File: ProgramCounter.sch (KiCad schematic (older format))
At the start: 8 parts, among them U13 74LS245, U14 74LS245, U15 74LS161, U16 74LS161, U17 74LS161, U18 74LS161

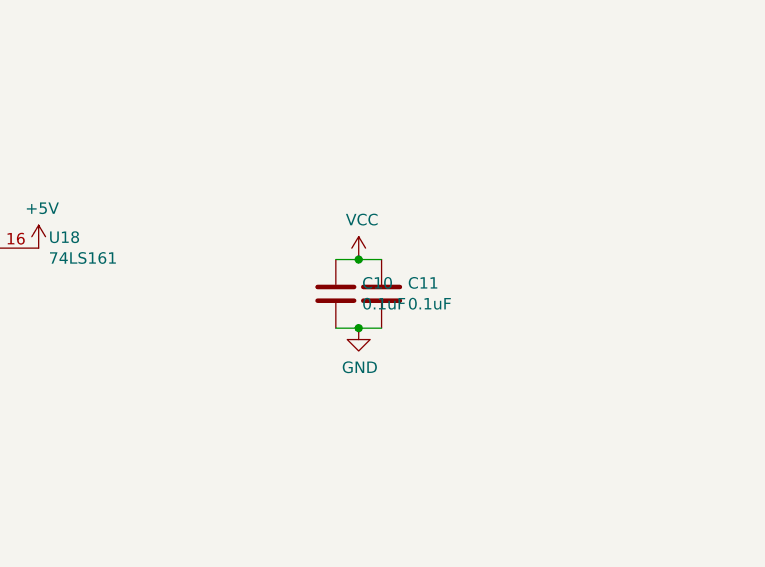
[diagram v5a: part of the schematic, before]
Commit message: added display
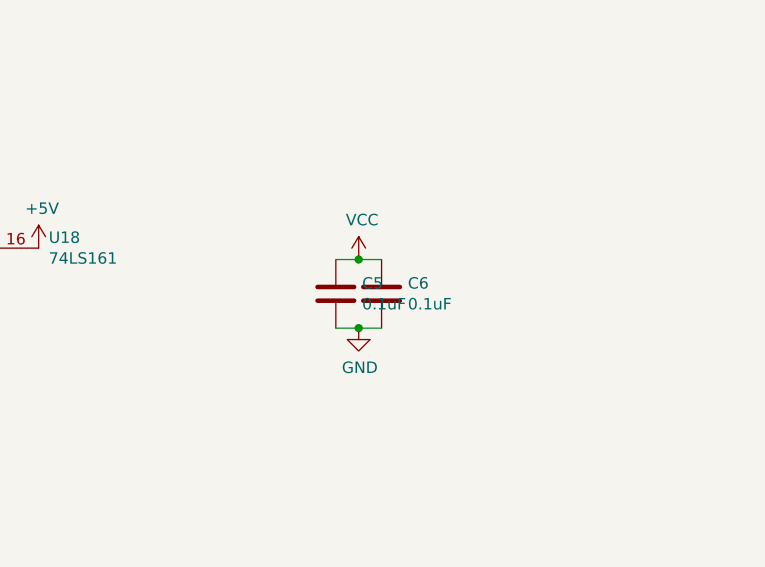
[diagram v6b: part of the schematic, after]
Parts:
- renumbered C10 to C5, C11 to C6
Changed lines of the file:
@@
 $Descr A3 16535 11693
 encoding utf-8
-Sheet 6 22
+Sheet 6 23
 Title ""
 Date ""
@@
 AR Path="/603B766D/5F6D5FCC" Ref="#PWR?"  Part="1"
 AR Path="/5F74778C/5F6D5FCC" Ref="#PWR?"  Part="1"
-AR Path="/5F6ACD14/5F6D5FCC" Ref="#PWR072"  Part="1"
-F 0 "#PWR072" H 4750 4200 50  0001 C CNN
+AR Path="/5F6ACD14/5F6D5FCC" Ref="#PWR050"  Part="1"
+F 0 "#PWR050" H 4750 4200 50  0001 C CNN
 F 1 "GND" H 4755 4277 50  0000 C CNN
 F 2 "" H 4750 4450 50  0001 C CNN
@@
 AR Path="/603B766D/5F6D5FF6" Ref="#PWR?"  Part="1"
 AR Path="/5F74778C/5F6D5FF6" Ref="#PWR?"  Part="1"
-AR Path="/5F6ACD14/5F6D5FF6" Ref="#PWR070"  Part="1"
-F 0 "#PWR070" H 3150 4300 50  0001 C CNN
+AR Path="/5F6ACD14/5F6D5FF6" Ref="#PWR048"  Part="1"
+F 0 "#PWR048" H 3150 4300 50  0001 C CNN
 F 1 "+5V" H 3165 4623 50  0000 C CNN
 F 2 "" H 3150 4450 50  0001 C CNN
@@
 AR Path="/603B766D/5F6D60A0" Ref="#PWR?"  Part="1"
 AR Path="/5F74778C/5F6D60A0" Ref="#PWR?"  Part="1"
-AR Path="/5F6ACD14/5F6D60A0" Ref="#PWR073"  Part="1"
-F 0 "#PWR073" H 4750 4200 50  0001 C CNN
+AR Path="/5F6ACD14/5F6D60A0" Ref="#PWR051"  Part="1"
+F 0 "#PWR051" H 4750 4200 50  0001 C CNN
 F 1 "GND" H 4755 4277 50  0000 C CNN
 F 2 "" H 4750 4450 50  0001 C CNN
@@
 AR Path="/603B766D/5F6D60B8" Ref="#PWR?"  Part="1"
 AR Path="/5F74778C/5F6D60B8" Ref="#PWR?"  Part="1"
-AR Path="/5F6ACD14/5F6D60B8" Ref="#PWR069"  Part="1"
-F 0 "#PWR069" H 3150 3400 50  0001 C CNN
+AR Path="/5F6ACD14/5F6D60B8" Ref="#PWR047"  Part="1"
+F 0 "#PWR047" H 3150 3400 50  0001 C CNN
 F 1 "GND" H 3155 3477 50  0000 C CNN
 F 2 "" H 3150 3650 50  0001 C CNN
@@
 AR Path="/603B766D/5F6D60C4" Ref="#PWR?"  Part="1"
 AR Path="/5F74778C/5F6D60C4" Ref="#PWR?"  Part="1"
-AR Path="/5F6ACD14/5F6D60C4" Ref="#PWR066"  Part="1"
-F 0 "#PWR066" H 1550 3500 50  0001 C CNN
+AR Path="/5F6ACD14/5F6D60C4" Ref="#PWR045"  Part="1"
+F 0 "#PWR045" H 1550 3500 50  0001 C CNN
 F 1 "+5V" H 1565 3823 50  0000 C CNN
 F 2 "" H 1550 3650 50  0001 C CNN
@@
 AR Path="/603B766D/5F6D60D0" Ref="#PWR?"  Part="1"
 AR Path="/5F74778C/5F6D60D0" Ref="#PWR?"  Part="1"
-AR Path="/5F6ACD14/5F6D60D0" Ref="#PWR071"  Part="1"
-F 0 "#PWR071" H 3150 4300 50  0001 C CNN
+AR Path="/5F6ACD14/5F6D60D0" Ref="#PWR049"  Part="1"
+F 0 "#PWR049" H 3150 4300 50  0001 C CNN
 F 1 "+5V" H 3165 4623 50  0000 C CNN
 F 2 "" H 3150 4450 50  0001 C CNN
@@
 AR Path="/603B766D/5F6D6186" Ref="#PWR?"  Part="1"
 AR Path="/5F74778C/5F6D6186" Ref="#PWR?"  Part="1"
-AR Path="/5F6ACD14/5F6D6186" Ref="#PWR067"  Part="1"
-F 0 "#PWR067" H 1550 3500 50  0001 C CNN
+AR Path="/5F6ACD14/5F6D6186" Ref="#PWR046"  Part="1"
+F 0 "#PWR046" H 1550 3500 50  0001 C CNN
 F 1 "+5V" H 1565 3823 50  0000 C CNN
 F 2 "" H 1550 3650 50  0001 C CNN
@@
 P 6900 4250
 AR Path="/5F9A8E46" Ref="#PWR?"  Part="1"
-AR Path="/5F6ACD14/5F9A8E46" Ref="#PWR075"  Part="1"
-F 0 "#PWR075" H 6900 4100 50  0001 C CNN
+AR Path="/5F6ACD14/5F9A8E46" Ref="#PWR053"  Part="1"
+F 0 "#PWR053" H 6900 4100 50  0001 C CNN
 F 1 "+5V" H 6915 4423 50  0000 C CNN
 F 2 "" H 6900 4250 50  0001 C CNN
@@
 P 8850 4400
 AR Path="/5F9B1DDA" Ref="#PWR?"  Part="1"
-AR Path="/5F6ACD14/5F9B1DDA" Ref="#PWR077"  Part="1"
-F 0 "#PWR077" H 8850 4250 50  0001 C CNN
+AR Path="/5F6ACD14/5F9B1DDA" Ref="#PWR055"  Part="1"
+F 0 "#PWR055" H 8850 4250 50  0001 C CNN
 F 1 "+5V" H 8865 4573 50  0000 C CNN
 F 2 "" H 8850 4400 50  0001 C CNN
@@
 P 10700 4450
 AR Path="/5F9BCAE2" Ref="#PWR?"  Part="1"
-AR Path="/5F6ACD14/5F9BCAE2" Ref="#PWR079"  Part="1"
-F 0 "#PWR079" H 10700 4300 50  0001 C CNN
+AR Path="/5F6ACD14/5F9BCAE2" Ref="#PWR057"  Part="1"
+F 0 "#PWR057" H 10700 4300 50  0001 C CNN
 F 1 "+5V" H 10715 4623 50  0000 C CNN
 F 2 "" H 10700 4450 50  0001 C CNN
@@
 P 12550 4450
 AR Path="/5F9BD87F" Ref="#PWR?"  Part="1"
-AR Path="/5F6ACD14/5F9BD87F" Ref="#PWR081"  Part="1"
-F 0 "#PWR081" H 12550 4300 50  0001 C CNN
+AR Path="/5F6ACD14/5F9BD87F" Ref="#PWR059"  Part="1"
+F 0 "#PWR059" H 12550 4300 50  0001 C CNN
 F 1 "+5V" H 12565 4623 50  0000 C CNN
 F 2 "" H 12550 4450 50  0001 C CNN
@@
 P 5300 4450
 AR Path="/5F9BEDE2" Ref="#PWR?"  Part="1"
-AR Path="/5F6ACD14/5F9BEDE2" Ref="#PWR074"  Part="1"
-F 0 "#PWR074" H 5300 4200 50  0001 C CNN
+AR Path="/5F6ACD14/5F9BEDE2" Ref="#PWR052"  Part="1"
+F 0 "#PWR052" H 5300 4200 50  0001 C CNN
 F 1 "GND" H 5305 4277 50  0000 C CNN
 F 2 "" H 5300 4450 50  0001 C CNN
@@
 P 7250 4450
 AR Path="/5F9C426E" Ref="#PWR?"  Part="1"
-AR Path="/5F6ACD14/5F9C426E" Ref="#PWR076"  Part="1"
-F 0 "#PWR076" H 7250 4200 50  0001 C CNN
+AR Path="/5F6ACD14/5F9C426E" Ref="#PWR054"  Part="1"
+F 0 "#PWR054" H 7250 4200 50  0001 C CNN
 F 1 "GND" H 7255 4277 50  0000 C CNN
 F 2 "" H 7250 4450 50  0001 C CNN
@@
 P 9100 4450
 AR Path="/5F9CE333" Ref="#PWR?"  Part="1"
-AR Path="/5F6ACD14/5F9CE333" Ref="#PWR078"  Part="1"
-F 0 "#PWR078" H 9100 4200 50  0001 C CNN
+AR Path="/5F6ACD14/5F9CE333" Ref="#PWR056"  Part="1"
+F 0 "#PWR056" H 9100 4200 50  0001 C CNN
 F 1 "GND" H 9105 4277 50  0000 C CNN
 F 2 "" H 9100 4450 50  0001 C CNN
@@
 P 10950 4450
 AR Path="/5F9D8AA1" Ref="#PWR?"  Part="1"
-AR Path="/5F6ACD14/5F9D8AA1" Ref="#PWR080"  Part="1"
-F 0 "#PWR080" H 10950 4200 50  0001 C CNN
+AR Path="/5F6ACD14/5F9D8AA1" Ref="#PWR058"  Part="1"
+F 0 "#PWR058" H 10950 4200 50  0001 C CNN
 F 1 "GND" H 10955 4277 50  0000 C CNN
 F 2 "" H 10950 4450 50  0001 C CNN
@@
 P 13950 4500
 AR Path="/5FB038A7" Ref="#PWR?"  Part="1"
-AR Path="/5F6ACD14/5FB038A7" Ref="#PWR0263"  Part="1"
-F 0 "#PWR0263" H 13950 4350 50  0001 C CNN
+AR Path="/5F6ACD14/5FB038A7" Ref="#PWR060"  Part="1"
+F 0 "#PWR060" H 13950 4350 50  0001 C CNN
 F 1 "VCC" H 13965 4673 50  0000 C CNN
 F 2 "" H 13950 4500 50  0001 C CNN
@@
 AR Path="/5FB038AD" Ref="#PWR?"  Part="1"
 AR Path="/5F75E433/5FB038AD" Ref="#PWR?"  Part="1"
-AR Path="/5F6ACD14/5FB038AD" Ref="#PWR0264"  Part="1"
-F 0 "#PWR0264" H 13950 4550 50  0001 C CNN
+AR Path="/5F6ACD14/5FB038AD" Ref="#PWR061"  Part="1"
+F 0 "#PWR061" H 13950 4550 50  0001 C CNN
 F 1 "GND" H 13955 4627 50  0000 C CNN
 F 2 "" H 13950 4800 50  0001 C CNN
@@
 P 13850 4650
 AR Path="/5F75E433/5FB038B5" Ref="C?"  Part="1"
-AR Path="/5F6ACD14/5FB038B5" Ref="C10"  Part="1"
-F 0 "C10" H 13965 4696 50  0000 L CNN
+AR Path="/5F6ACD14/5FB038B5" Ref="C5"  Part="1"
+F 0 "C5" H 13965 4696 50  0000 L CNN
 F 1 "0.1uF" H 13965 4605 50  0000 L CNN
 F 2 "Capacitor_THT:CP_Axial_L10.0mm_D4.5mm_P15.00mm_Horizontal" H 13888 4500 50  0001 C CNN
@@
 P 14050 4650
 AR Path="/5F75E433/5FB038BF" Ref="C?"  Part="1"
-AR Path="/5F6ACD14/5FB038BF" Ref="C11"  Part="1"
-F 0 "C11" H 14165 4696 50  0000 L CNN
+AR Path="/5F6ACD14/5FB038BF" Ref="C6"  Part="1"
+F 0 "C6" H 14165 4696 50  0000 L CNN
 F 1 "0.1uF" H 14165 4605 50  0000 L CNN
 F 2 "Capacitor_THT:CP_Axial_L10.0mm_D4.5mm_P15.00mm_Horizontal" H 14088 4500 50  0001 C CNN

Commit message: clean up
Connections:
- wire segments 243 -> 222
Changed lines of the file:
@@
 Wire Wire Line
 	9400 2750 11250 2750
-Connection ~ 11250 2750
-Wire Wire Line
-	11250 2750 15650 2750
 Wire Wire Line
 	1150 2750 5600 2750
@@
 Wire Wire Line
 	11750 3950 11750 2650
-Connection ~ 11750 2650
-Wire Wire Line
-	11750 2650 15650 2650
 Wire Wire Line
 	5800 3950 5800 750
-Connection ~ 5800 750
-Wire Wire Line
-	5800 750  15650 750
 Text HLabel 1150 2850 0    50   Input ~ 0
 CE
@@
 Wire Wire Line
 	11650 3900 11650 3950
-Connection ~ 11600 2850
-Wire Wire Line
-	11600 2850 15650 2850
 Wire Wire Line
 	11600 3900 11550 3900
@@
 Wire Wire Line
 	4450 5150 4450 4950
-Connection ~ 5050 2950
-Wire Wire Line
-	5050 2950 15650 2950
 Wire Wire Line
 	6600 3950 6600 1000
-Connection ~ 6600 1000
-Wire Wire Line
-	6600 1000 15650 1000
 Wire Wire Line
 	6500 3950 6500 1100
-Connection ~ 6500 1100
-Wire Wire Line
-	6500 1100 15650 1100
 Wire Wire Line
 	6400 3950 6400 1200
-Connection ~ 6400 1200
-Wire Wire Line
-	6400 1200 15650 1200
 Wire Wire Line
 	6300 3950 6300 1300
-Connection ~ 6300 1300
-Wire Wire Line
-	6300 1300 15650 1300
-Connection ~ 8550 1400
 Wire Wire Line
 	8450 1500 8450 3950
-Connection ~ 8450 1500
-Wire Wire Line
-	8450 1500 15650 1500
 Wire Wire Line
 	8350 1600 8350 3950
-Connection ~ 8350 1600
-Wire Wire Line
-	8350 1600 15650 1600
 Connection ~ 8550 3950
 Wire Wire Line
@@
 Wire Wire Line
 	2550 1700 8250 1700
-Connection ~ 8250 1700
-Wire Wire Line
-	8250 1700 15650 1700
-Wire Wire Line
-	8550 1400 15650 1400
 Wire Wire Line
 	8250 3950 8250 1700
@@
 Wire Wire Line
 	10400 3950 10400 1800
-Connection ~ 10400 1800
-Wire Wire Line
-	10400 1800 15650 1800
 Wire Wire Line
 	10300 3950 10300 1900
-Connection ~ 10300 1900
-Wire Wire Line
-	10300 1900 15650 1900
 Wire Wire Line
 	10200 3950 10200 2000
-Connection ~ 10200 2000
-Wire Wire Line
-	10200 2000 15650 2000
 Wire Wire Line
 	10100 3950 10100 2100
-Connection ~ 10100 2100
-Wire Wire Line
-	10100 2100 15650 2100
 Wire Wire Line
 	12250 3950 12250 2200
-Connection ~ 12250 2200
-Wire Wire Line
-	12250 2200 15650 2200
 Wire Wire Line
 	12150 3950 12150 2300
-Connection ~ 12150 2300
-Wire Wire Line
-	12150 2300 15650 2300
 Wire Wire Line
 	12050 3950 12050 2400
 Wire Wire Line
 	4050 2400 12050 2400
-Connection ~ 12050 2400
-Wire Wire Line
-	12050 2400 15650 2400
 Wire Wire Line
 	11950 3950 11950 2500
 Wire Wire Line
 	4150 2500 11950 2500
-Connection ~ 11950 2500
-Wire Wire Line
-	11950 2500 15650 2500
 Wire Wire Line
 	6900 4450 6900 4250
